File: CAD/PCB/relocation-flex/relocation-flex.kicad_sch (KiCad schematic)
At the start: 27 parts, among them IC1 BH7240AKV-E2, J1 SBUS_DATA, J10 ANLG_RGB, J2 SBUS_ADDR, J3 SBUS_CTRL, J4 DVID_RED, J5 DVID_GRN, J6 DVID_BLU, J7 DVID_CTRL, J8 VDAC_PWR, J9 62684-402100ALF, U1 LM1881

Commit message: reloc - finish BIOS relocation schematic & begin SPU relocation schematic
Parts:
- added IC2: SST39VF040-70-4C-WHE, SOP50P1400X120-32N, symbol SST39VF040-70-4C-WHE:SST39VF040-70-4C-WHE
- added U2: M11B416256A-35J, symbol psx-spu:M11B416256A-35J
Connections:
- net A0: now also IC2.20 (A0), U2.16 (A0)
- net A1: now also IC2.19 (A1), U2.17 (A1)
- net A10: now also IC2.31 (A10)
- net A11: now also IC2.1 (A11)
- net A12: now also IC2.12 (A12)
- net A13: now also IC2.4 (A13)
- net A14: now also IC2.5 (A14)
- net A15: now also IC2.11 (A15)
- net A16: now also IC2.10 (A16)
- net A17: now also IC2.6 (A17)
- net A18: now also IC2.9 (A18)
- net A2: now also IC2.18 (A2), U2.18 (A2)
- net A3: now also IC2.17 (A3), U2.19 (A3)
- net A4: now also IC2.16 (A4), U2.22 (A4)
- net A5: now also IC2.15 (A5), U2.23 (A5)
- net A6: now also IC2.14 (A6), U2.24 (A6)
- net A7: now also IC2.13 (A7), U2.25 (A7)
- net A8: now also IC2.3 (A8), U2.26 (A8)
- net A9: now also IC2.2 (A9)
- net CS2: now also IC2.30 (CE#)
- net GND: now also IC2.24 (VSS), U2.21 (GND), U2.35 (GND), U2.40 (GND)
- net IRQ1: now also IC2.32 (OE#)
- net SWR0: now also IC2.7 (WE#)
- new net: U2.11 (NC), U2.12 (NC), U2.15 (NC), U2.30 (NC)
- new net +3.5V: IC2.8 (VDD), U2.1 (VCC), U2.20 (VCC), U2.6 (VCC)
- new net DQ0: IC2.21 (DQ0)
- new net DQ1: IC2.22 (DQ1)
- new net DQ2: IC2.23 (DQ2)
- new net DQ3: IC2.25 (DQ3)
- new net DQ4: IC2.26 (DQ4)
- new net DQ5: IC2.27 (DQ5)
- new net DQ6: IC2.28 (DQ6)
- new net DQ7: IC2.29 (DQ7)
- new net I/O1: U2.2 (I/O1)
- new net I/O10: U2.32 (I/O10)
- new net I/O11: U2.33 (I/O11)
- new net I/O12: U2.34 (I/O12)
- new net I/O13: U2.36 (I/O13)
- new net I/O14: U2.37 (I/O14)
- new net I/O15: U2.38 (I/O15)
- new net I/O16: U2.39 (I/O16)
- new net I/O2: U2.3 (I/O2)
- new net I/O3: U2.4 (I/O3)
- new net I/O4: U2.5 (I/O4)
- new net I/O5: U2.7 (I/O5)
- new net I/O6: U2.8 (I/O6)
- new net I/O7: U2.9 (I/O7)
- new net I/O8: U2.10 (I/O8)
- new net I/O9: U2.31 (I/O9)
- no-connect marks 8 -> 9
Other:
- note added: "BIOS Flash"
- moved on the sheet: C1, C2, C3, C4, C5, C6, C7, C8, C9, IC1, J10, J4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

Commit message: reloc - finish SPU relocation schematic
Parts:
- added C10: 1uF, symbol Device:C_Small
- added C11, C12, C13, C14, C15, C16, C17, C18: 100nF, symbol Device:C_Small
- added R7: 220Ω, symbol Device:R_Small
- added U3: CXD2925Q, symbol psx-spu:CXD2925Q
- renumbered IC2 to U1, IC1 to U4, U1 to U5
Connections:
- net +5V is gone; now on net +3.5V: C7.2, C8.2, C9.2, J8.1 (Pin_1), R6.1, U4.13 (NT/PAL), U4.20 (DVDD), U4.47 (AVCC1), U4.9 (AVCC2), U5.8 (VCC)
- net DQ0 is gone; now on net SD0: U1.21 (DQ0)
- net DQ1 is gone; now on net SD1: U1.22 (DQ1)
- net DQ2 is gone; now on net SD2: U1.23 (DQ2)
- net DQ3 is gone; now on net SD3: U1.25 (DQ3)
- net DQ4 is gone; now on net SD4: U1.26 (DQ4)
- net DQ5 is gone; now on net SD5: U1.27 (DQ5)
- net DQ6 is gone; now on net SD6: U1.28 (DQ6)
- net DQ7 is gone; now on net SD7: U1.29 (DQ7)
- net +3.5V: now also C11.1, C12.1, C13.1, C14.1, C15.1, C16.1, C17.1, C18.1, U3.28 (VCC), U3.3 (VCC), U3.53 (VCC), U3.79 (VCC)
- net CS4: now also U3.31 (~{SPU})
- net DACK4: now also U3.34 (DACK)
- net DREQ4: now also U3.36 (DREQ)
- net GND: now also C10.2, C11.2, C12.2, C13.2, C14.2, C15.2, C16.2, C17.2, C18.2, U3.15 (GND), U3.29 (GND), U3.4 (GND), U3.40 (GND), U3.42 (GND), U3.54 (GND), U3.65 (GND), U3.78 (GND), U3.88 (GND), U3.90 (GND)
- net RST: now also C10.1, R7.1
- net SRD: now also U3.32 (~{RD})
- net SWR0: now also U3.33 (~{WR})
- net MWE: now reaches U2.13 (~{WE})
- net MWE: now also U3.84 (~{WE0})
- net MRAS: now reaches U2.14 (~{RAS})
- net MRAS: now also U3.63 (~{RAS})
- net MOE: now reaches U2.27 (~{OE})
- net MOE: now also U3.85 (~{OE0})
- net MCAS: now reaches U2.28 (~{UCAS})
- net MCAS: now also U2.29 (~{LCAS}), U3.64 (~{CAS})
- net A0 renamed SA0
- net SA0: no longer U2.16 (A0)
- net A1 renamed SA1
- net SA1: now also U3.20 (SA1); no longer U2.17 (A1)
- net A10 renamed SA10
- net A11 renamed SA11
- net A12 renamed SA12
- net A13 renamed SA13
- net A14 renamed SA14
- net A15 renamed SA15
- net A16 renamed SA16
- net A17 renamed SA17
- net A18 renamed SA18
- net A19 renamed SA19
- net A2 renamed SA2
- net SA2: now also U3.21 (SA2); no longer U2.18 (A2)
- net A3 renamed SA3
- net SA3: now also U3.22 (SA3); no longer U2.19 (A3)
- net A4 renamed SA4
- net SA4: now also U3.23 (SA4); no longer U2.22 (A4)
- net A5 renamed SA5
- net SA5: now also U3.24 (SA5); no longer U2.23 (A5)
- net A6 renamed SA6
- net SA6: now also U3.25 (SA6); no longer U2.24 (A6)
- net A7 renamed SA7
- net SA7: now also U3.26 (SA7); no longer U2.25 (A7)
- net A8 renamed SA8
- net SA8: now also U3.27 (SA8); no longer U2.26 (A8)
- net A9 renamed SA9
- net SA9: now also U3.30 (SA9)
- net D0 renamed SD0
- net SD0: now also U3.1 (SD0)
- net D1 renamed SD1
- net SD1: now also U3.2 (SD1)
- net D10 renamed SD10
- net SD10: now also U3.13 (SD10)
- net D11 renamed SD11
- net SD11: now also U3.14 (SD11)
- net D12 renamed SD12
- net SD12: now also U3.16 (SD12)
- net D13 renamed SD13
- net SD13: now also U3.17 (SD13)
- net D14 renamed SD14
- net SD14: now also U3.18 (SD14)
- net D15 renamed SD15
- net SD15: now also U3.19 (SD15)
- net D2 renamed SD2
- net SD2: now also U3.5 (SD2)
- net D3 renamed SD3
- net SD3: now also U3.6 (SD3)
- net D4 renamed SD4
- net SD4: now also U3.7 (SD4)
- net D5 renamed SD5
- net SD5: now also U3.8 (SD5)
- net D6 renamed SD6
- net SD6: now also U3.9 (SD6)
- net D7 renamed SD7
- net SD7: now also U3.10 (SD7)
- net D8 renamed SD8
- net SD8: now also U3.11 (SD8)
- net D9 renamed SD9
- net SD9: now also U3.12 (SD9)
- net I/O1 renamed MD0
- net MD0: now also U3.62 (MD0)
- net I/O10 renamed MD9
- net MD9: now also U3.51 (MD9)
- net I/O11 renamed MD10
- net MD10: now also U3.50 (MD10)
- net I/O12 renamed MD11
- net MD11: now also U3.49 (MD11)
- net I/O13 renamed MD12
- net MD12: now also U3.48 (MD12)
- net I/O14 renamed MD13
- net MD13: now also U3.47 (MD13)
- net I/O15 renamed MD14
- net MD14: now also U3.46 (MD14)
- net I/O16 renamed MD15
- net MD15: now also U3.45 (MD15)
- net I/O2 renamed MD1
- net MD1: now also U3.61 (MD1)
- net I/O3 renamed MD2
- net MD2: now also U3.60 (MD2)
- net I/O4 renamed MD3
- net MD3: now also U3.59 (MD3)
- net I/O5 renamed MD4
- net MD4: now also U3.58 (MD4)
- net I/O6 renamed MD5
- net MD5: now also U3.57 (MD5)
- net I/O7 renamed MD6
- net MD6: now also U3.56 (MD6)
- net I/O8 renamed MD7
- net MD7: now also U3.55 (MD7)
- net I/O9 renamed MD8
- net MD8: now also U3.52 (MD8)
- net IRQ10 renamed IRQ9
- net IRQ9: now also U3.35 (~{IRQ})
- net SYSCLK renamed SYSCK
- net SYSCK: now also U3.41 (SYSCLK)
- new net: R7.2, U3.38 (~{RST})
- new net BCIA: U3.91 (BCIA)
- new net BCIB: U3.94 (BCIB)
- new net BCKO: U3.97 (BCKO)
- new net DATO: U3.99 (DATO)
- new net DTIA: U3.93 (DTIA)
- new net DTIB: U3.96 (DTIB)
- new net LRCO: U3.98 (LRCO)
- new net LRIA: U3.92 (LRIA)
- new net LRIB: U3.95 (LRIB)
- new net MA1: U2.16 (A0), U3.82 (MA1)
- new net MA2: U2.17 (A1), U3.81 (MA2)
- new net MA3: U2.18 (A2), U3.80 (MA3)
- new net MA4: U2.19 (A3), U3.77 (MA4)
- new net MA5: U2.22 (A4), U3.76 (MA5)
- new net MA6: U2.23 (A5), U3.75 (MA6)
- new net MA7: U2.24 (A6), U3.74 (MA7)
- new net MA8: U2.25 (A7), U3.73 (MA8)
- new net MA9: U2.26 (A8), U3.72 (MA9)
- new net XCK: U3.89 (XCK)
- now unconnected: U2.11 (NC), U2.12 (NC), U2.15 (NC), U2.30 (NC)
- no-connect marks 9 -> 17
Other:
- note added: "SPU Relocation"
- moved on the sheet: J1, J2, J3, J9, U2

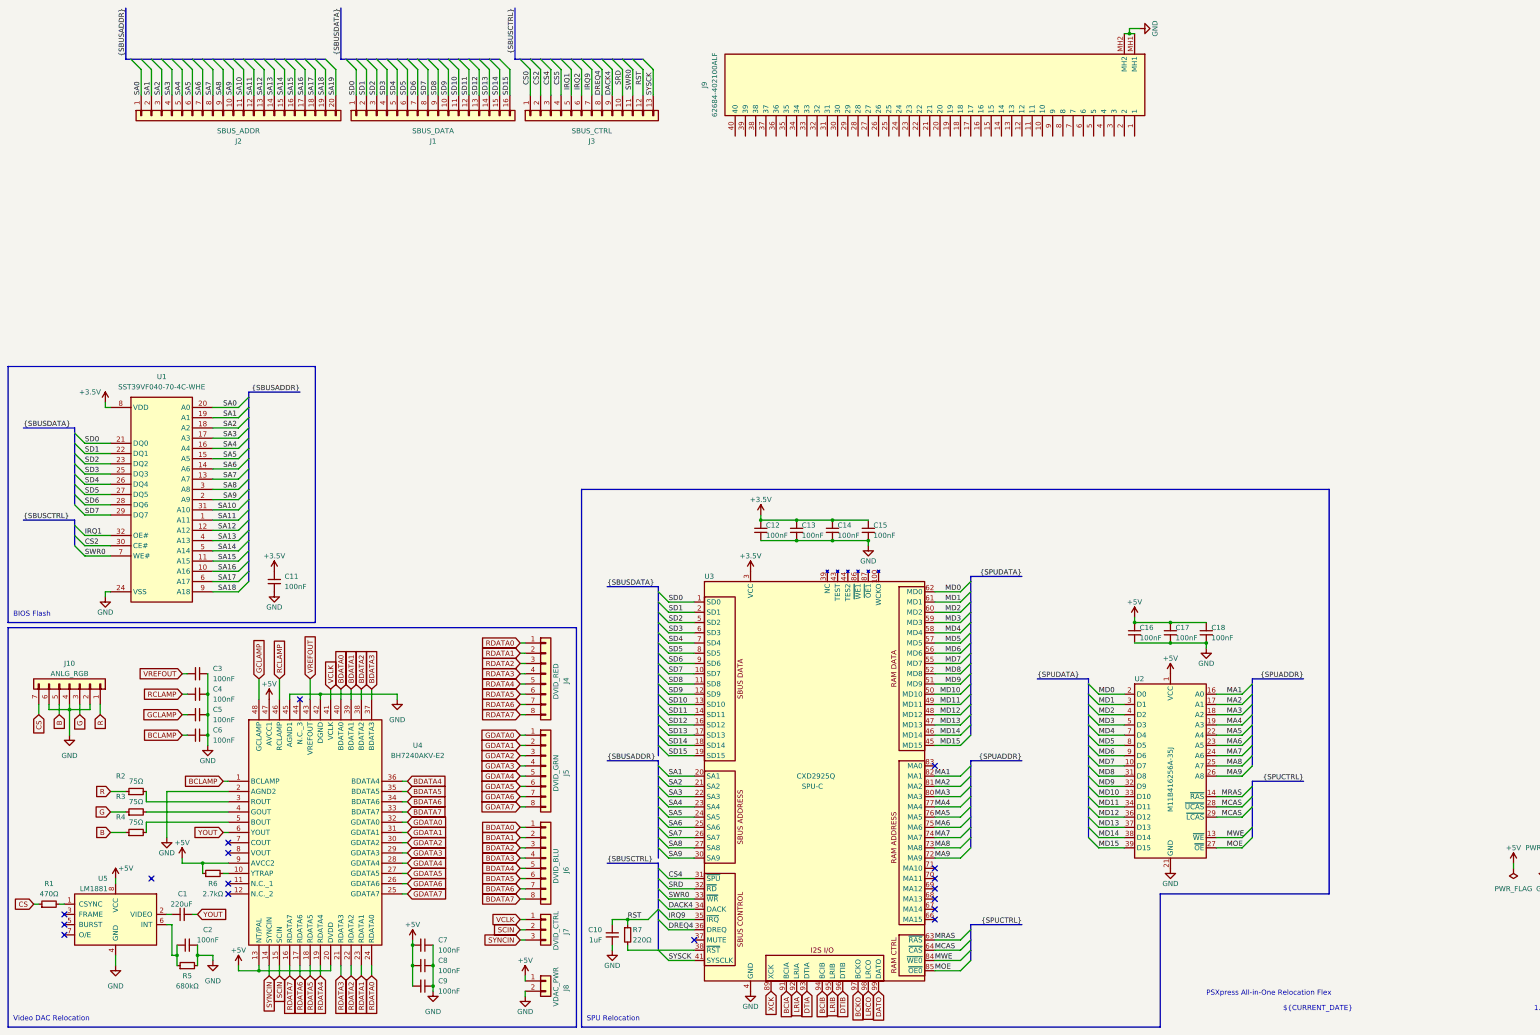
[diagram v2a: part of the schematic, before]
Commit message: reloc - finish flex schematic and add finishing touches to psio qsb
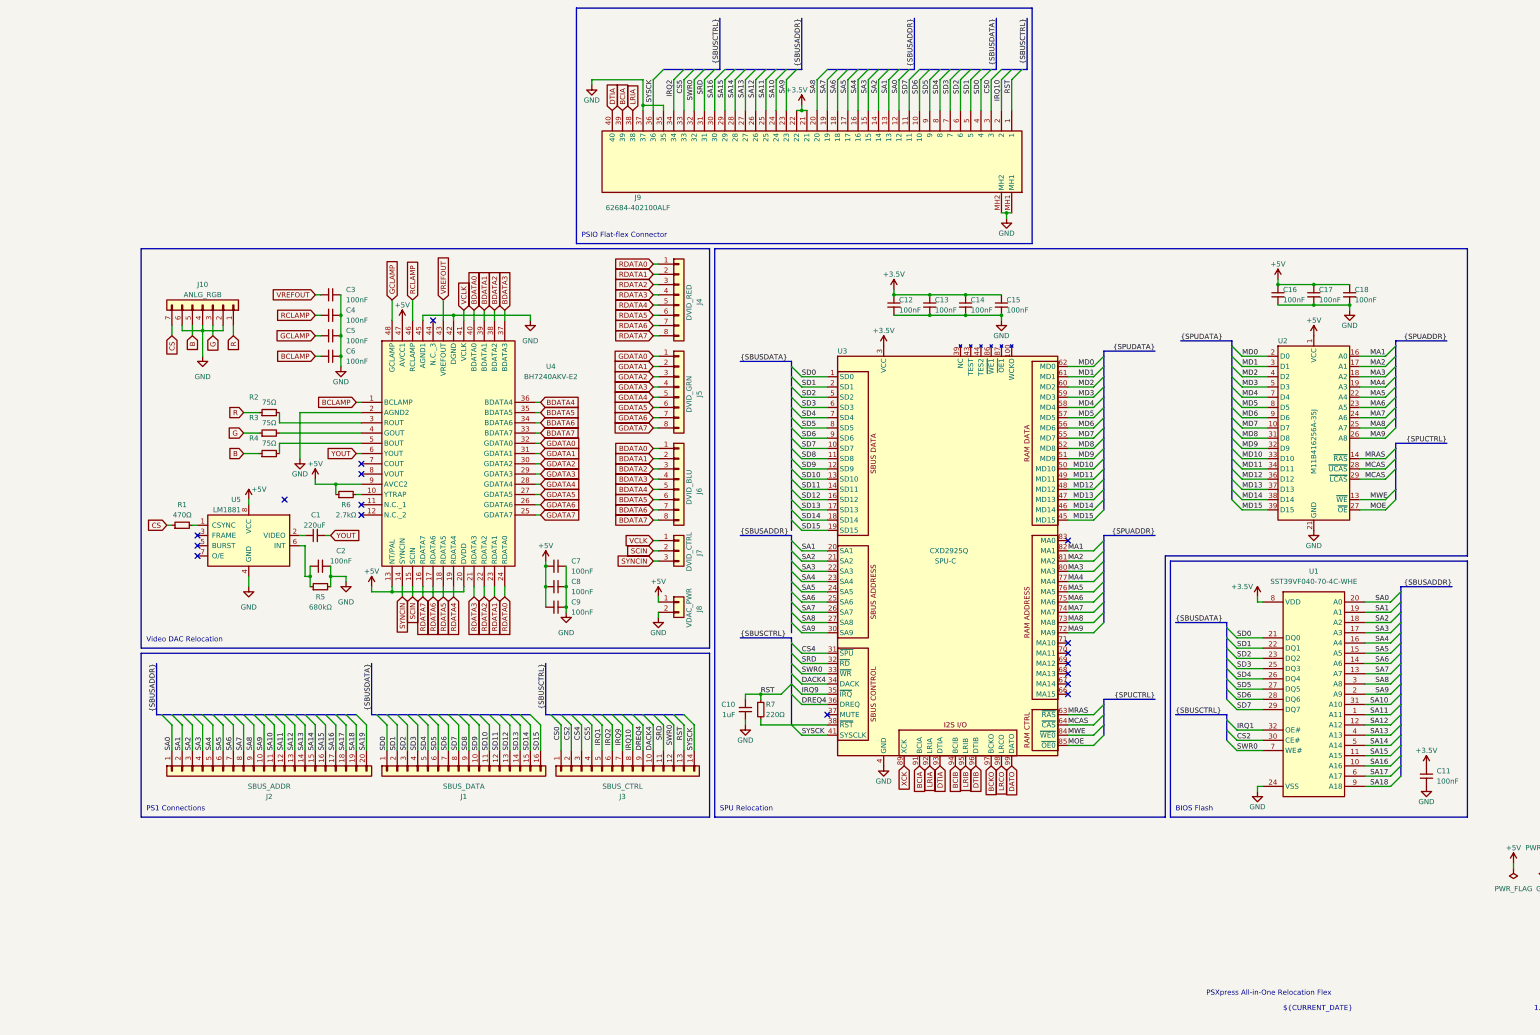
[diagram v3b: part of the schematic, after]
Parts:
- J3: symbol Connector_Generic:Conn_01x13 -> Connector_Generic:Conn_01x14
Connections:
- net +3.5V: now also J9.21, J9.22
- net BCIA: now also J9.39
- net CS0: now also J9.3
- net CS5: now also J9.33
- net DACK4: now also J3.10 (Pin_10); no longer J3.9 (Pin_9)
- net DREQ4: now also J3.9 (Pin_9); no longer J3.8 (Pin_8)
- net DTIA: now also J9.40
- net GND: now also J9.35, J9.37
- net IRQ2: now also J9.34
- net LRIA: now also J9.38
- net RST: now also J3.13 (Pin_13), J9.1; no longer J3.12 (Pin_12)
- net SA0: now also J9.12
- net SA1: now also J9.13
- net SA10: now also J9.24
- net SA11: now also J9.25
- net SA12: now also J9.26
- net SA13: now also J9.27
- net SA14: now also J9.28
- net SA15: now also J9.29
- net SA16: now also J9.30
- net SA2: now also J9.14
- net SA3: now also J9.15
- net SA4: now also J9.16
- net SA5: now also J9.17
- net SA6: now also J9.18
- net SA7: now also J9.19
- net SA8: now also J9.20
- net SA9: now also J9.23
- net SD0: now also J9.4
- net SD1: now also J9.5
- net SD2: now also J9.6
- net SD3: now also J9.7
- net SD4: now also J9.8
- net SD5: now also J9.9
- net SD6: now also J9.10
- net SD7: now also J9.11
- net SRD: now also J3.11 (Pin_11), J9.31; no longer J3.10 (Pin_10)
- net SWR0: now also J3.12 (Pin_12), J9.32; no longer J3.11 (Pin_11)
- net SYSCK: now also J3.14 (Pin_14), J9.36; no longer J3.13 (Pin_13)
- net IRQ10: now reaches J9.2
- net IRQ10: now also J3.8 (Pin_8)
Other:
- note added: "PS1 Connections"
- note added: "PSIO Flat-flex Connector"
- moved on the sheet: C1, C10, C11, C12, C13, C14, C15, C16, C17, C18, C2, C3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
